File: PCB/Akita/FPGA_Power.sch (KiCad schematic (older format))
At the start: 1 part

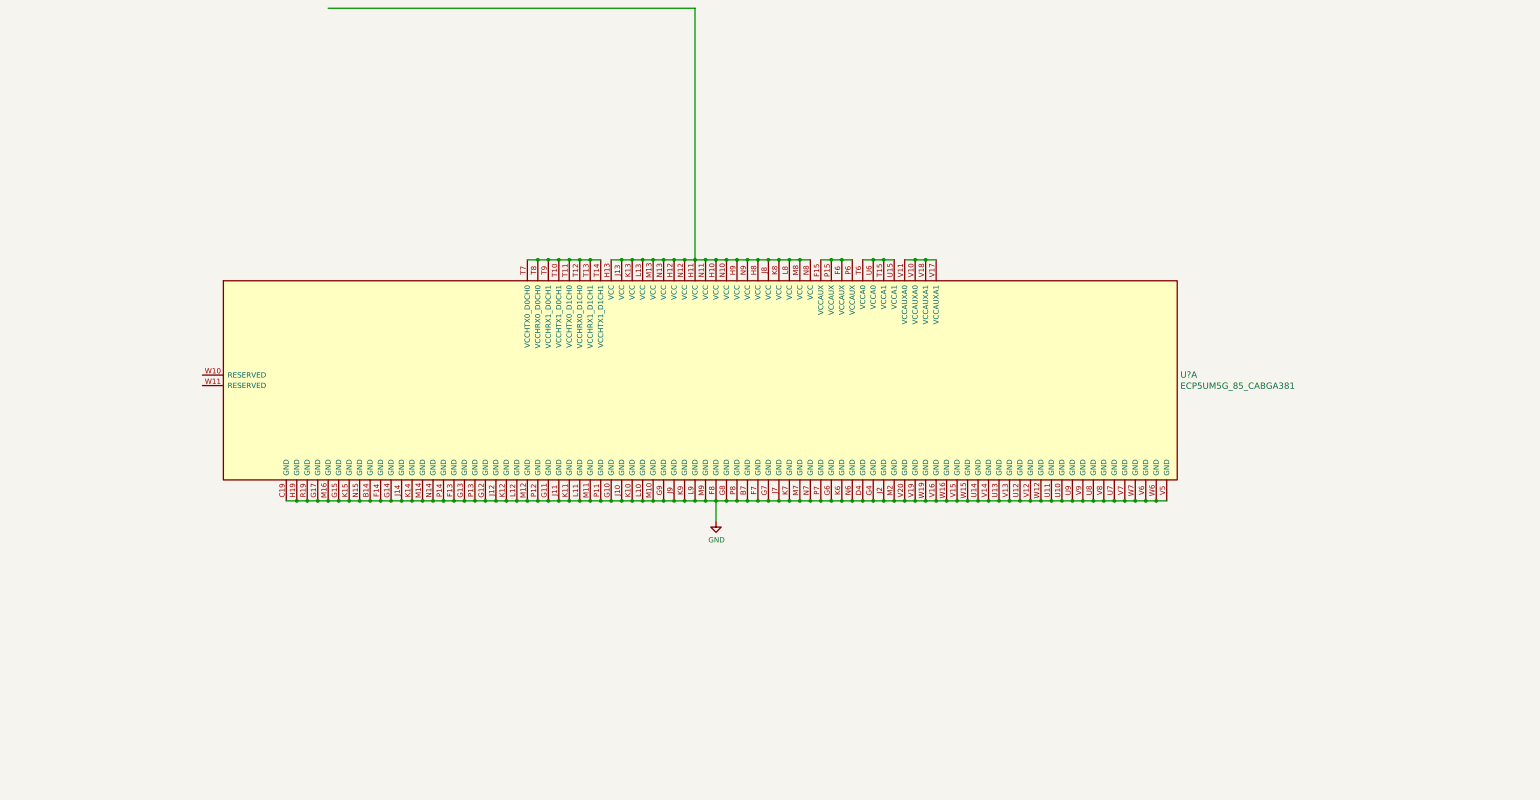
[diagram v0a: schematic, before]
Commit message: Symbols and Power Schematic
Power for FPGA schematic laid out, schematic symbols for resistors and caps replaced with standard ones.
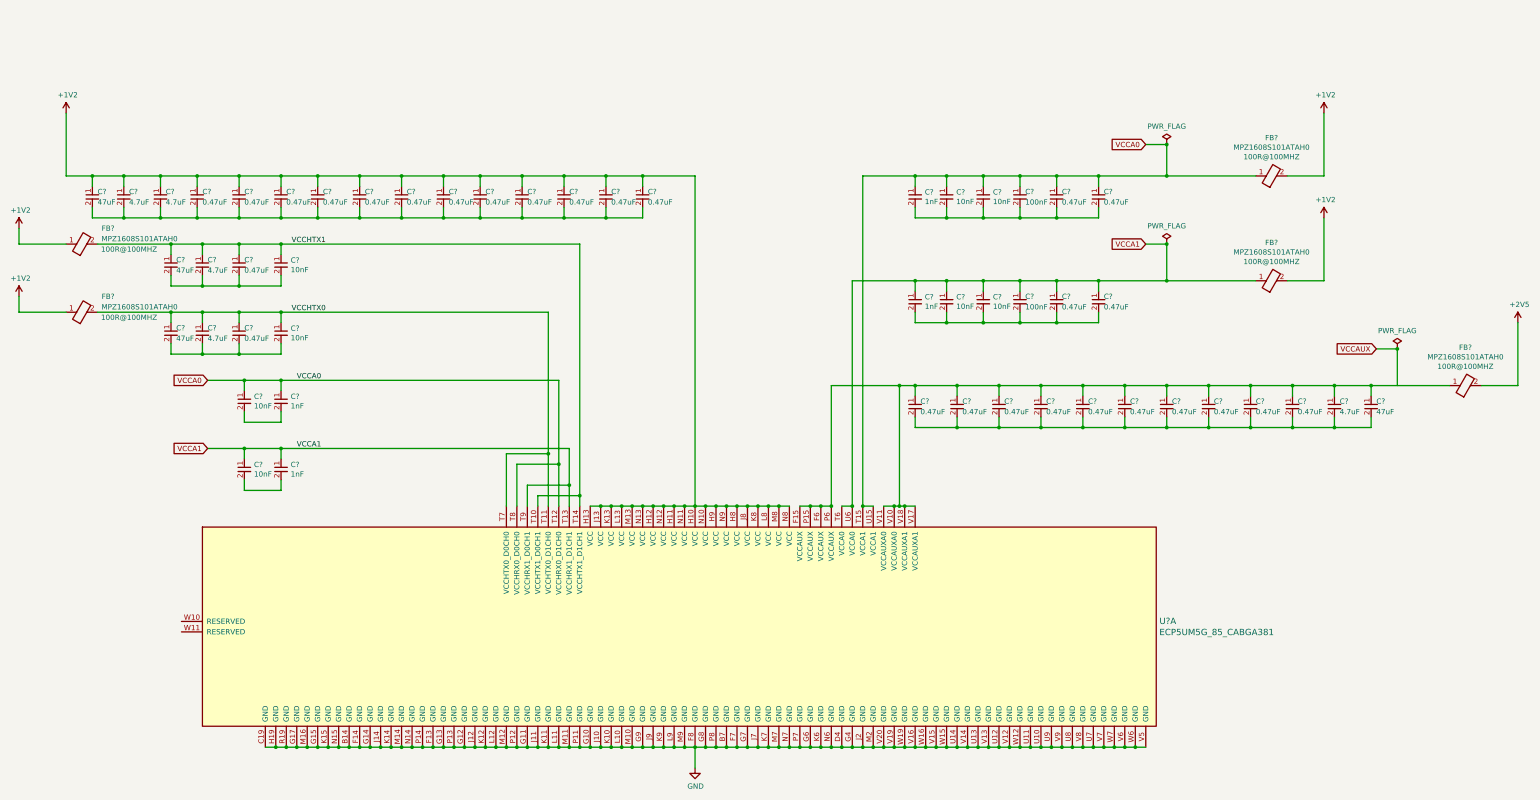
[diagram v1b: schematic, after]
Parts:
- added C? (x4): CL05B102KB5NNNC, Capacitors_SMD:C_0402_NoSilk, symbol Akita_Pro_Library:CL05B102KB5NNNC
- added C? (x8): CL05B103KB5NNNC, Capacitors_SMD:C_0402_NoSilk, symbol Akita_Pro_Library:CL05B103KB5NNNC
- added C? (x4): CL21A476MQYNNNE, Capacitors_SMD:C_0805, symbol Akita_Pro_Library:CL21A476MQYNNNE
- added C? (x5): CL10A475KP8NNNC, Capacitors_SMD:C_0603, symbol Akita_Pro_Library:CL10A475KP8NNNC
- added C? (x28): CL05A474KQ5NNNC, Capacitors_SMD:C_0402_NoSilk, symbol Akita_Pro_Library:CL05A474KQ5NNNC
- added C? (x2): CL05B104KO5NNNC, Capacitors_SMD:C_0402_NoSilk, symbol Akita_Pro_Library:CL05B104KO5NNNC
- added FB? (x5): MPZ1608S101ATAH0, Resistors_SMD:R_0603, symbol Akita_Pro_Library:MPZ1608S101ATAH0
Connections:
- net at U?.F15 (VCCAUX), U?.F6 (VCCAUX), U?.P15 (VCCAUX)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: now also U?.V10 (VCCAUXA0), U?.V11 (VCCAUXA0), U?.V17 (VCCAUXA1), U?.V18 (VCCAUXA1), C?.1, C?.1, C?.1, C?.1, C?.1, C?.1, C?.1, C?.1, C?.1, C?.1, C?.1, C?.1, FB?.1
- net +1V2: now reaches U?.H10 (VCC), U?.H11 (VCC), U?.H12 (VCC), U?.H13 (VCC), U?.H8 (VCC), U?.H9 (VCC), U?.J13 (VCC), U?.J8 (VCC), U?.K13 (VCC), U?.K8 (VCC), U?.L13 (VCC), U?.L8 (VCC), U?.M13 (VCC), U?.M8 (VCC), U?.N10 (VCC), U?.N11 (VCC), U?.N12 (VCC), U?.N13 (VCC), U?.N8 (VCC), U?.N9 (VCC)
- net +1V2: now also C?.1, C?.1, C?.1, C?.1, C?.1, C?.1, C?.1, C?.1, C?.1, C?.1, C?.1, C?.1, C?.1, C?.1, C?.1, FB?.1, FB?.1, FB?.2, FB?.2
- net VCCA0: now reaches U?.T15 (VCCA1), U?.U15 (VCCA1)
- net VCCA0: now also U?.T12 (VCCHRX0_D1CH0), U?.T8 (VCCHRX0_D0CH0), C?.1, C?.1, C?.1, C?.1, C?.1, C?.1, C?.1, C?.1, FB?.1; no longer U?.T6 (VCCA0), U?.U6 (VCCA0)
- new net: C?.2, C?.2 (x2)
- new net: C?.2, C?.2, C?.2, C?.2 (x2)
- new net: C?.2, C?.2, C?.2, C?.2, C?.2, C?.2, C?.2, C?.2, C?.2, C?.2, C?.2, C?.2, C?.2, C?.2, C?.2
- new net: C?.2, C?.2, C?.2, C?.2, C?.2, C?.2 (x2)
- new net: C?.2, C?.2, C?.2, C?.2, C?.2, C?.2, C?.2, C?.2, C?.2, C?.2, C?.2, C?.2
- new net +2V5: FB?.2
- new net VCCA1: C?.1, C?.1, C?.1, C?.1, C?.1, C?.1, C?.1, C?.1, FB?.1, U?.T13 (VCCHRX1_D1CH1), U?.T6 (VCCA0), U?.T9 (VCCHRX1_D0CH1), U?.U6 (VCCA0)
- new net VCCHTX0: C?.1, C?.1, C?.1, C?.1, FB?.2, U?.T11 (VCCHTX0_D1CH0), U?.T7 (VCCHTX0_D0CH0)
- new net VCCHTX1: C?.1, C?.1, C?.1, C?.1, FB?.2, U?.T10 (VCCHTX1_D0CH1), U?.T14 (VCCHTX1_D1CH1)
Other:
- moved on the sheet: U?A
